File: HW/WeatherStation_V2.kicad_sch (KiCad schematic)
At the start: 62 parts, among them J1 Sensors + PWR, J10 BATTERY, J2 I2C, J3 DHT, J4 I2C, J5 GPIO2, J6 I2C, J7 I2C, J8 GPIO, J9 PROG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

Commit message: Updated PCB - DRC OK
DRC without any error;
some small improvements in scheme
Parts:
- removed J8: GPIO, Connector_PinHeader_2.54mm:PinHeader_1x10_P2.54mm_Vertical, symbol Connector:Conn_01x10_Pin
- renumbered J10 to J8
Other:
- moved on the sheet: GPIO1, J5

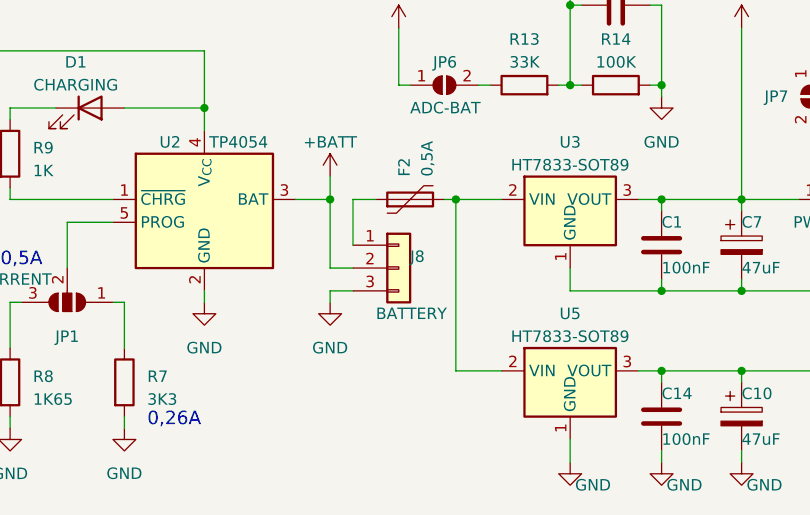
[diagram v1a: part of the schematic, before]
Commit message: 3 pin battery connector updated to 2 pin
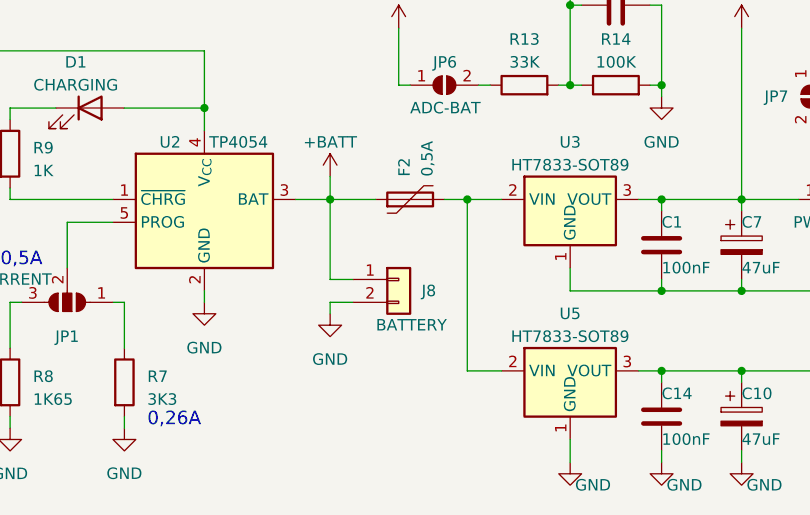
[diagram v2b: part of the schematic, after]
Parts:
- removed J8: BATTERY, Connector_JST:JST_XH_B3B-XH-A_1x03_P2.50mm_Vertical, symbol Connector_Generic:Conn_01x03
- added J8: BATTERY, Connector_JST:JST_XH_B2B-XH-A_1x02_P2.50mm_Vertical, symbol Connector_Generic:Conn_01x02
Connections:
- net +BATT: now also F2.1, J8.1 (Pin_1)
- net GND: now also J8.2 (Pin_2)
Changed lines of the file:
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@@
   (junction (at 36.83 40.64) (diameter 0) (color 0 0 0 0)
   )
-  (junction (at 124.46 163.83) (diameter 0) (color 0 0 0 0)
-  )
   (junction (at 29.21 163.83) (diameter 0) (color 0 0 0 0)
   )
@@
   (junction (at 147.32 173.99) (diameter 0) (color 0 0 0 0)
   )
-  (junction (at 110.49 163.83) (diameter 0) (color 0 0 0 0)
+  (junction (at 125.73 163.83) (diameter 0) (color 0 0 0 0)
   )
   (junction (at 137.16 151.13) (diameter 0) (color 0 0 0 0)
@@
   (junction (at 269.24 55.88) (diameter 0) (color 0 0 0 0)
   )
+  (junction (at 110.49 163.83) (diameter 0) (color 0 0 0 0)
+  )
   (junction (at 185.42 132.08) (diameter 0) (color 0 0 0 0)
   )
@@
     (stroke (width 0) (type default))
   )
-  (wire (pts (xy 110.49 171.45) (xy 113.03 171.45))
-    (stroke (width 0) (type default))
-  )
   (wire (pts (xy 118.11 33.02) (xy 118.11 34.29))
     (stroke (width 0) (type default))
@@
     (stroke (width 0) (type default))
   )
-  (wire (pts (xy 113.03 163.83) (xy 115.57 163.83))
+  (wire (pts (xy 110.49 163.83) (xy 115.57 163.83))
     (stroke (width 0) (type default))
   )
@@
     (stroke (width 0) (type default))
   )
+  (wire (pts (xy 110.49 175.26) (xy 113.03 175.26))
+    (stroke (width 0) (type default))
+  )
   (wire (pts (xy 146.05 85.09) (xy 151.13 85.09))
     (stroke (width 0) (type default))
@@
     (stroke (width 0) (type default))
   )
+  (wire (pts (xy 110.49 172.72) (xy 110.49 163.83))
+    (stroke (width 0) (type default))
+  )
   (wire (pts (xy 214.63 44.45) (xy 214.63 45.72))
     (stroke (width 0) (type default))
@@
     (stroke (width 0) (type default))
   )
-  (wire (pts (xy 124.46 163.83) (xy 129.54 163.83))
-    (stroke (width 0) (type default))
-  )
   (wire (pts (xy 36.83 27.94) (xy 36.83 33.02))
     (stroke (width 0) (type default))
@@
     (stroke (width 0) (type default))
   )
+  (wire (pts (xy 123.19 163.83) (xy 125.73 163.83))
+    (stroke (width 0) (type default))
+  )
   (wire (pts (xy 254 60.96) (xy 254 73.66))
     (stroke (width 0) (type default))
@@
     (stroke (width 0) (type default))
   )
-  (wire (pts (xy 113.03 168.91) (xy 113.03 163.83))
-    (stroke (width 0) (type default))
-  )
   (wire (pts (xy 208.28 45.72) (xy 214.63 45.72))
     (stroke (width 0) (type default))
@@
     (stroke (width 0) (type default))
   )
-  (wire (pts (xy 124.46 163.83) (xy 124.46 182.88))
+  (wire (pts (xy 125.73 163.83) (xy 125.73 182.88))
     (stroke (width 0) (type default))
   )
@@
     (stroke (width 0) (type default))
   )
-  (wire (pts (xy 110.49 173.99) (xy 110.49 175.26))
-    (stroke (width 0) (type default))
-  )
-  (wire (pts (xy 110.49 173.99) (xy 113.03 173.99))
-    (stroke (width 0) (type default))
-  )
   (wire (pts (xy 217.17 115.57) (xy 222.25 115.57))
     (stroke (width 0) (type default))
@@
     (stroke (width 0) (type default))
   )
-  (wire (pts (xy 124.46 182.88) (xy 129.54 182.88))
+  (wire (pts (xy 125.73 182.88) (xy 129.54 182.88))
     (stroke (width 0) (type default))
   )
@@
     (stroke (width 0) (type default))
   )
-  (wire (pts (xy 123.19 163.83) (xy 124.46 163.83))
-    (stroke (width 0) (type default))
-  )
   (wire (pts (xy 36.83 33.02) (xy 36.83 40.64))
     (stroke (width 0) (type default))
@@
     (stroke (width 0) (type default))
   )
+  (wire (pts (xy 125.73 163.83) (xy 129.54 163.83))
+    (stroke (width 0) (type default))
+  )
   (wire (pts (xy 208.28 17.78) (xy 214.63 17.78))
     (stroke (width 0) (type default))
@@
     (stroke (width 0) (type default))
   )
-  (wire (pts (xy 110.49 163.83) (xy 110.49 171.45))
-    (stroke (width 0) (type default))
-  )
   (wire (pts (xy 154.94 50.8) (xy 147.32 50.8))
     (stroke (width 0) (type default))
@@
     (stroke (width 0) (type default))
   )
+  (wire (pts (xy 110.49 175.26) (xy 110.49 176.53))
+    (stroke (width 0) (type default))
+  )
+  (wire (pts (xy 113.03 172.72) (xy 110.49 172.72))
+    (stroke (width 0) (type default))
+  )
   (wire (pts (xy 195.58 77.47) (xy 195.58 78.74))
     (stroke (width 0) (type default))
@@
     )
   )
-  (symbol (lib_id "Connector_Generic:Conn_01x03") (at 118.11 171.45 0) (unit 1)
-    (in_bom yes) (on_board yes) (dnp no)
-    (property "Reference" "J8" (at 119.38 170.18 0)
-      (effects (font (size 1.27 1.27)) (justify left))
-    )
-    (property "Value" "BATTERY" (at 115.57 176.53 0)
-      (effects (font (size 1.27 1.27)) (justify left))
-    )
-    (property "Footprint" "Connector_JST:JST_XH_B3B-XH-A_1x03_P2.50mm_Vertical" (at 118.11 171.45 0)
-      (effects (font (size 1.27 1.27)) hide)
-    )
-    (property "Datasheet" "~" (at 118.11 171.45 0)
-      (effects (font (size 1.27 1.27)) hide)
-    )
-    (pin "1")
-    (pin "2")
-    (pin "3")
-    (instances
-      (project "WeatherStation_V2"
-        (path "/229ea4f7-2e31-48a9-a37f-daf3a6855339"
-          (reference "J8") (unit 1)
-        )
-      )
-    )
-  )
   (symbol (lib_id "Device:R") (at 227.33 24.13 90) (unit 1)
     (in_bom yes) (on_board yes) (dnp no) (fields_autoplaced)
@@
     )
   )
+  (symbol (lib_id "Connector_Generic:Conn_01x02") (at 118.11 172.72 0) (unit 1)
+    (in_bom yes) (on_board yes) (dnp no)
+    (property "Reference" "J8" (at 120.65 173.99 0)
+      (effects (font (size 1.27 1.27)) (justify left))
+    )
+    (property "Value" "BATTERY" (at 115.57 177.8 0)
+      (effects (font (size 1.27 1.27)) (justify left))
+    )
+    (property "Footprint" "Connector_JST:JST_XH_B2B-XH-A_1x02_P2.50mm_Vertical" (at 118.11 172.72 0)
+      (effects (font (size 1.27 1.27)) hide)
+    )
+    (property "Datasheet" "~" (at 118.11 172.72 0)
+      (effects (font (size 1.27 1.27)) hide)
+    )
+    (pin "1")
+    (pin "2")
+    (instances
+      (project "WeatherStation_V2"
+        (path "/229ea4f7-2e31-48a9-a37f-daf3a6855339"
+          (reference "J8") (unit 1)
+        )
+      )
+    )
+  )
   (symbol (lib_id "Device:LED") (at 83.82 153.67 0) (unit 1)
     (in_bom yes) (on_board yes) (dnp no) (fields_autoplaced)
@@
     )
   )
-  (symbol (lib_name "GND_7") (lib_id "power:GND") (at 110.49 175.26 0) (unit 1)
-    (in_bom yes) (on_board yes) (dnp no) (fields_autoplaced)
-    (property "Reference" "#PWR025" (at 110.49 181.61 0)
-      (effects (font (size 1.27 1.27)) hide)
-    )
-    (property "Value" "GND" (at 110.49 180.34 0)
-      (effects (font (size 1.27 1.27)))
-    )
-    (property "Footprint" "" (at 110.49 175.26 0)
-      (effects (font (size 1.27 1.27)) hide)
-    )
-    (property "Datasheet" "" (at 110.49 175.26 0)
-      (effects (font (size 1.27 1.27)) hide)
-    )
-    (pin "1")
-    (instances
-      (project "WeatherStation_V2"
-        (path "/229ea4f7-2e31-48a9-a37f-daf3a6855339"
-          (reference "#PWR025") (unit 1)
-        )
-      )
-    )
-  )
   (symbol (lib_id "Connector:Conn_01x03_Pin") (at 243.84 134.62 0) (unit 1)
     (in_bom yes) (on_board yes) (dnp no) (fields_autoplaced)
@@
         )
       )
+    )
+  )
+  (symbol (lib_name "GND_7") (lib_id "power:GND") (at 110.49 176.53 0) (unit 1)
+    (in_bom yes) (on_board yes) (dnp no) (fields_autoplaced)
+    (property "Reference" "#PWR041" (at 110.49 182.88 0)
+      (effects (font (size 1.27 1.27)) hide)
+    )
+    (property "Value" "GND" (at 110.49 181.61 0)
+      (effects (font (size 1.27 1.27)))
+    )
+    (property "Footprint" "" (at 110.49 176.53 0)
+      (effects (font (size 1.27 1.27)) hide)
+    )
+    (property "Datasheet" "" (at 110.49 176.53 0)
+      (effects (font (size 1.27 1.27)) hide)
+    )
+    (pin "1")
+    (instances
+      (project "WeatherStation_V2"
+        (path "/229ea4f7-2e31-48a9-a37f-daf3a6855339"
+          (reference "#PWR041") (unit 1)
+        )
+      )
